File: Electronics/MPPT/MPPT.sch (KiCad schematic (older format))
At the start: 94 parts, among them J1 Solar Array, J2 Battery, J3 Car Power, J4 CAN_In, J5 CAN_Out, Q1 200N25N, Q2 200N25N, SW1 RESET, SW2 CAN Address, U1 PDS1-S12-S9-M, U2 Nucleo_L432KC, U3 UCC37321, U4 INA213, U5 ADM3055E, U6 INA213, U7 CDSOT23-T24CAN

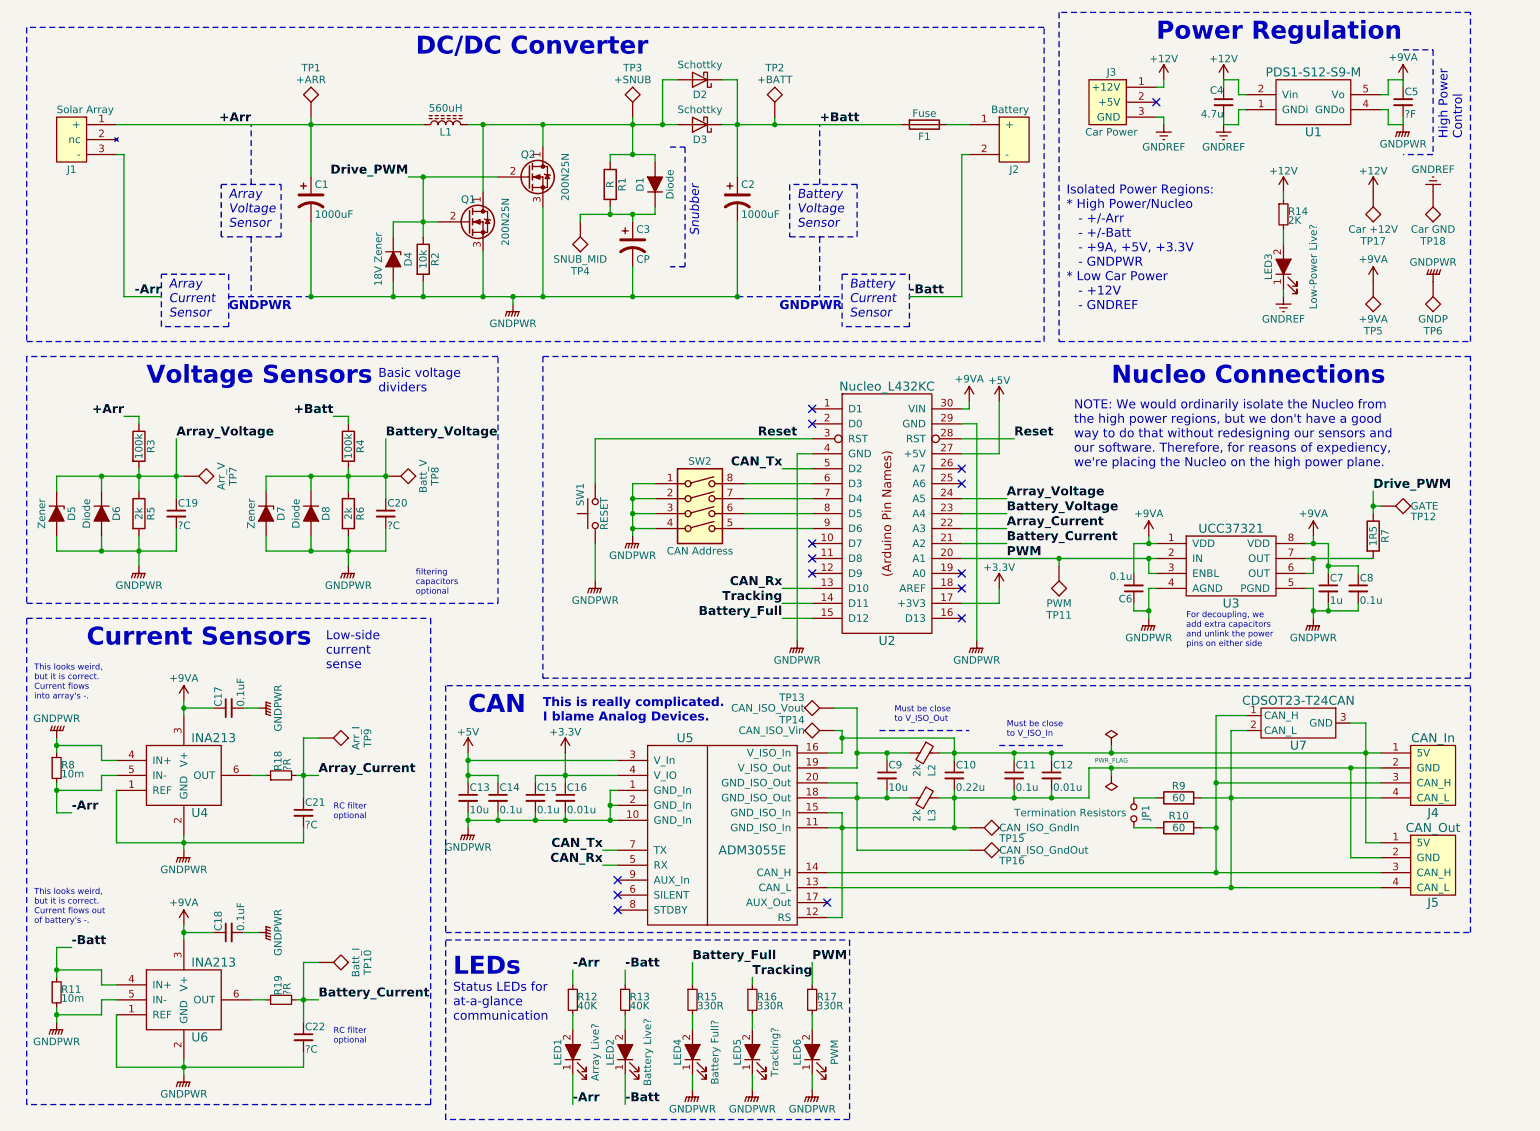
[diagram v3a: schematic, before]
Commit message: MPPT: Replaced power regulator with a 3W-output isolator.
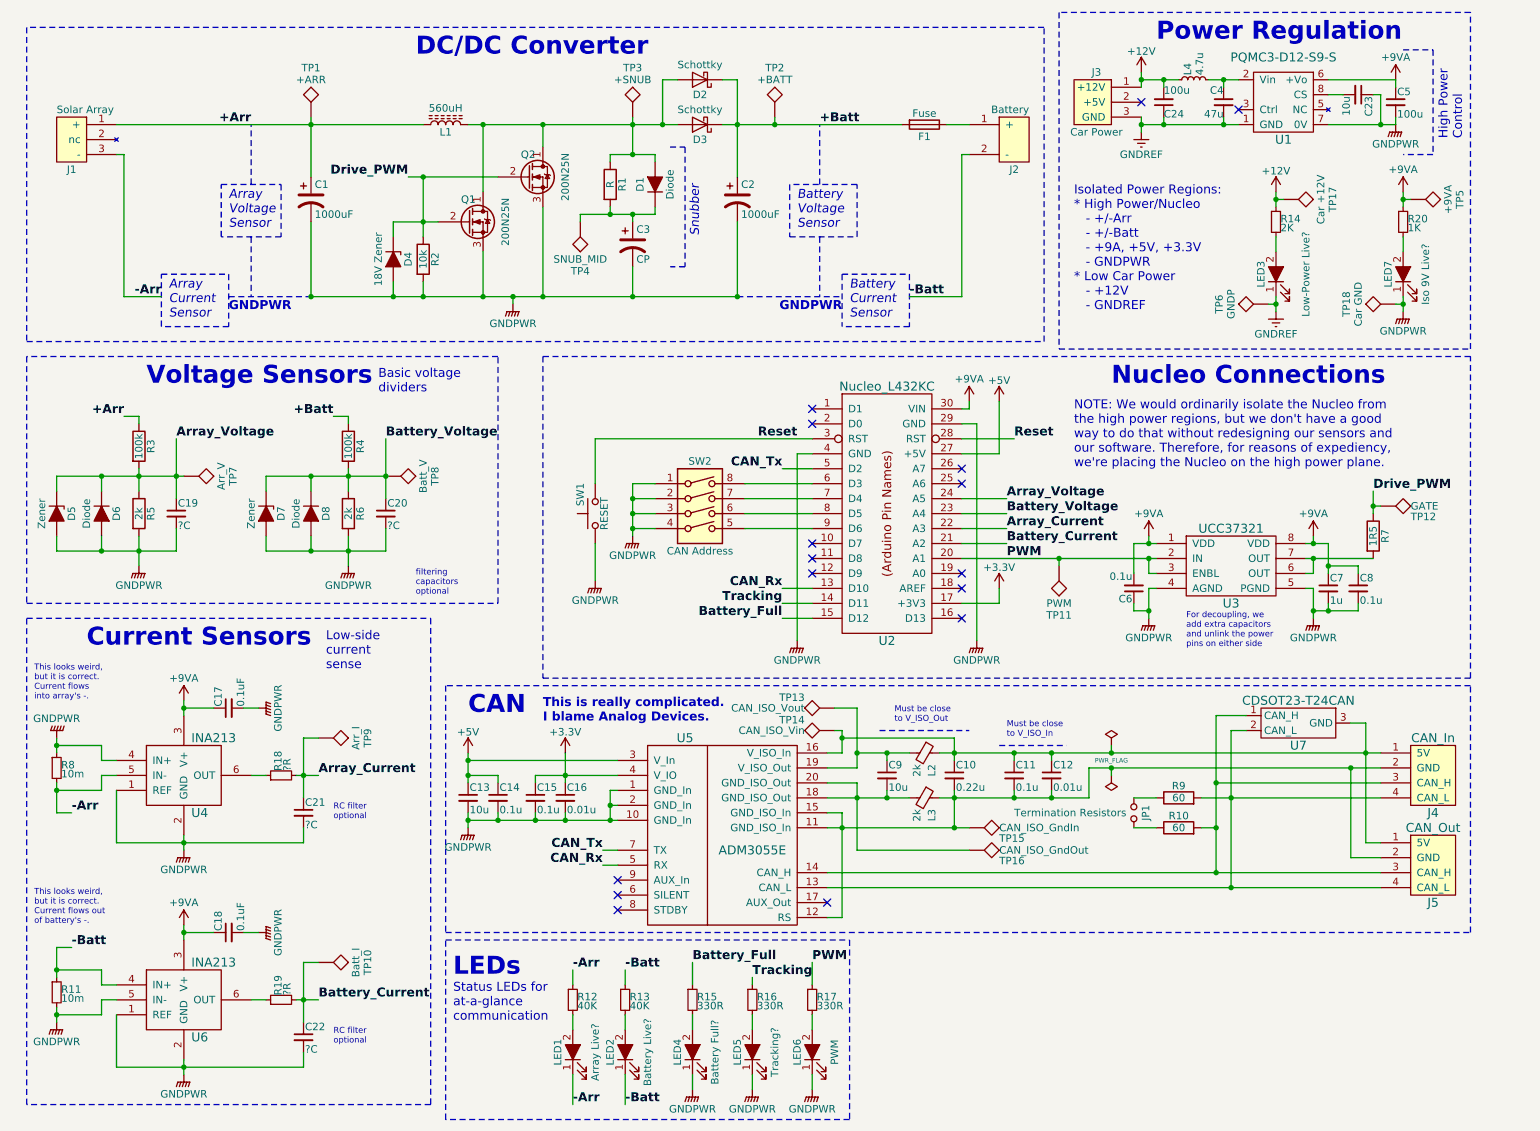
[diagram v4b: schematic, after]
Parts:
- removed U1: PDS1-S12-S9-M, UTSVT_ICs:PDS1-M, symbol PDS1-S12-S9-M
- added C23: 10u, Capacitors_SMD:C_0805_HandSoldering, symbol C_Small
- added C24: 100u, Capacitors_SMD:C_0805_HandSoldering, symbol C_Small
- added L4: 4.7u, Inductors_SMD:L_0805_HandSoldering, symbol L_Small
- added LED7: Iso 9V Live?, LEDs:LED_0805_HandSoldering, symbol LED_ALT
- added R20: 1K, Resistors_SMD:R_0805_HandSoldering, symbol R_Small
- added U1: PQMC3-D12-S9-S, UTSVT_ICs:CUI_PQMC3-S, symbol PQMC3-Dx-Sx-S
- C4: value 4.7u -> 47u
- C5: value ?F -> 100u
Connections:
- net +12V: now also C24.2, L4.1; no longer C4.1
- net +9VA: now also R20.1, U1.6 (+Vo)
- net GNDPWR: now also TP18.1, C23.1, LED7.1 (K), U1.7 (0V); no longer TP6.1
- net GNDREF: now also TP6.1, C24.1, U1.1 (GND); no longer TP18.1
- new net: C4.1, L4.2, U1.2 (Vin)
- new net: C23.2, U1.8 (CS)
- new net: LED7.2 (A), R20.2
- no-connect marks 15 -> 16
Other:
- moved on the sheet: C5, J3, LED3, R14, TP17, TP18, TP5, TP6

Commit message: MPPT: Clean up and rearrange schematic
* Compacted and cleaned up the CAN and Power Regulation blocks.
* Spread blocks out a little more
* Swapped locations of CAN and Nucleo Connections blocks to allow more space for the LEDs block to expand.
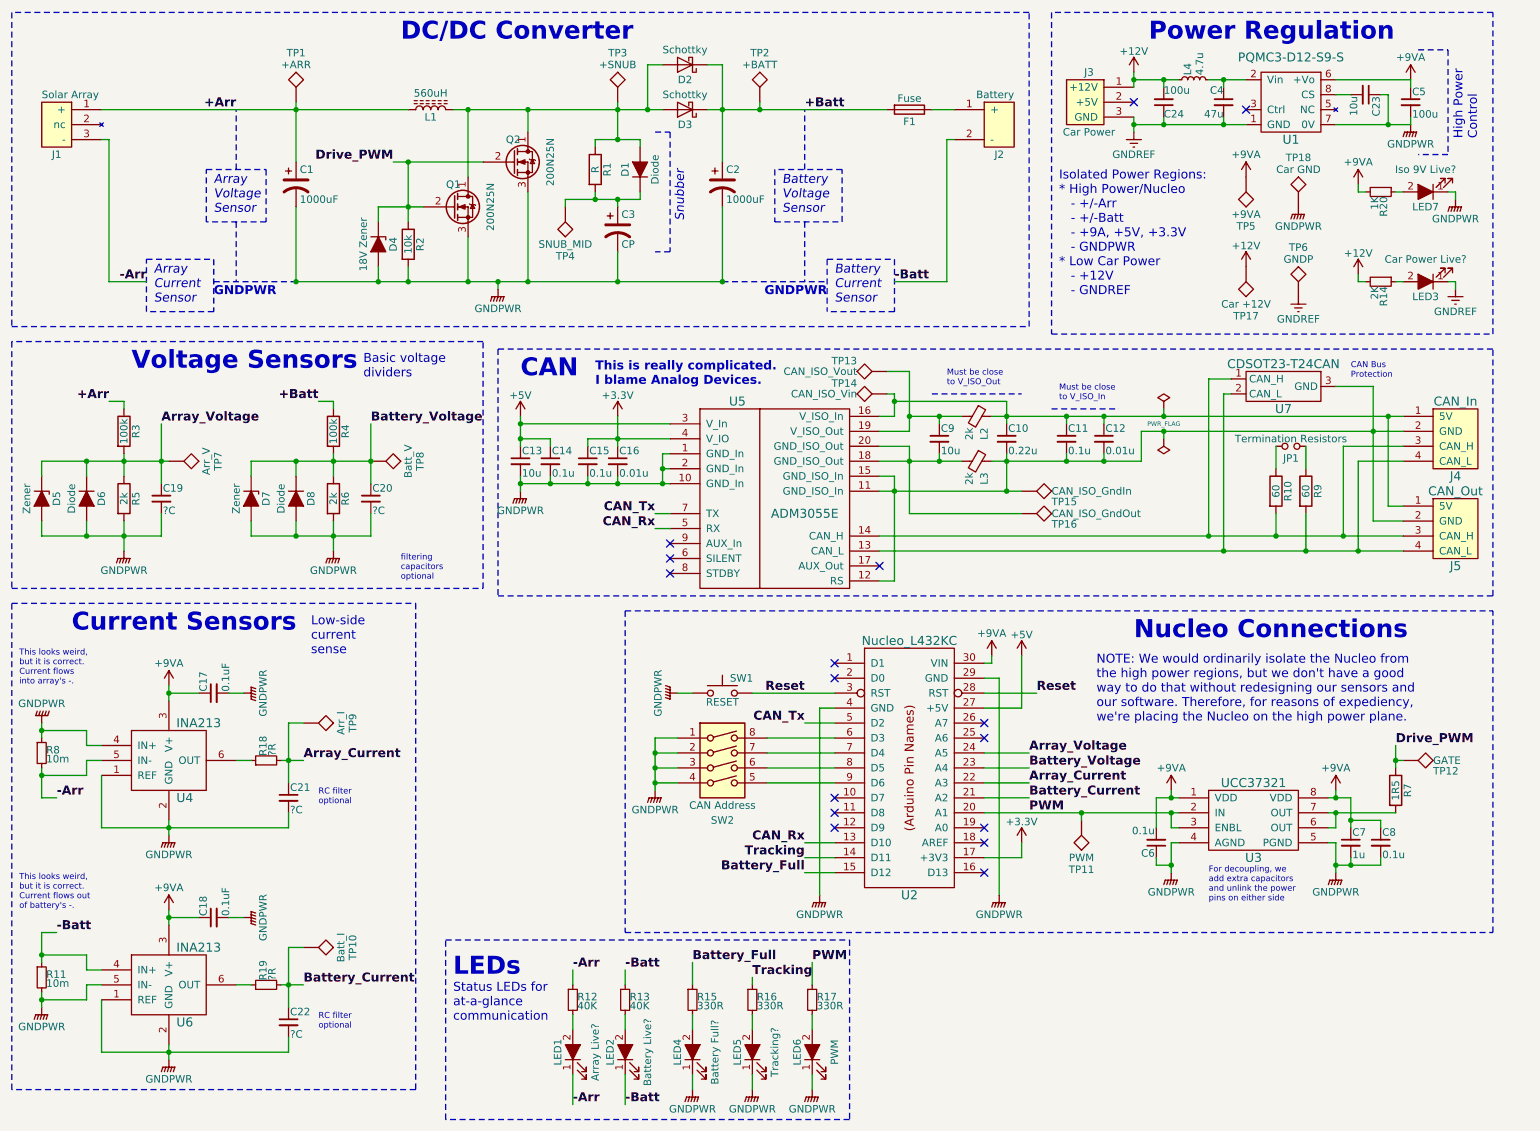
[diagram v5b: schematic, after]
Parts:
- LED3: value Low-Power Live? -> Car Power Live?
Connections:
- net +12V: now also R14.2; no longer R14.1
- net +9VA: now also R20.2; no longer R20.1
- net at C10.1, C11.1, C12.1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: no longer U7.3 (GND)
- net at C10.2, C11.2, C12.2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: now also U7.3 (GND)
- net at LED3.2 (A): now also R14.1; no longer R14.2
- net at LED7.2 (A): now also R20.1; no longer R20.2
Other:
- note added: "CAN Bus\nProtection"
- moved on the sheet: C1, C10, C11, C12, C13, C14, C15, C16, C17, C18, C19, C2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

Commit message: MPPT: Add CAN_Tx/Rx LEDs and TPs; move power LEDs to LEDs block
Also nudged some blocks and circuitry around.
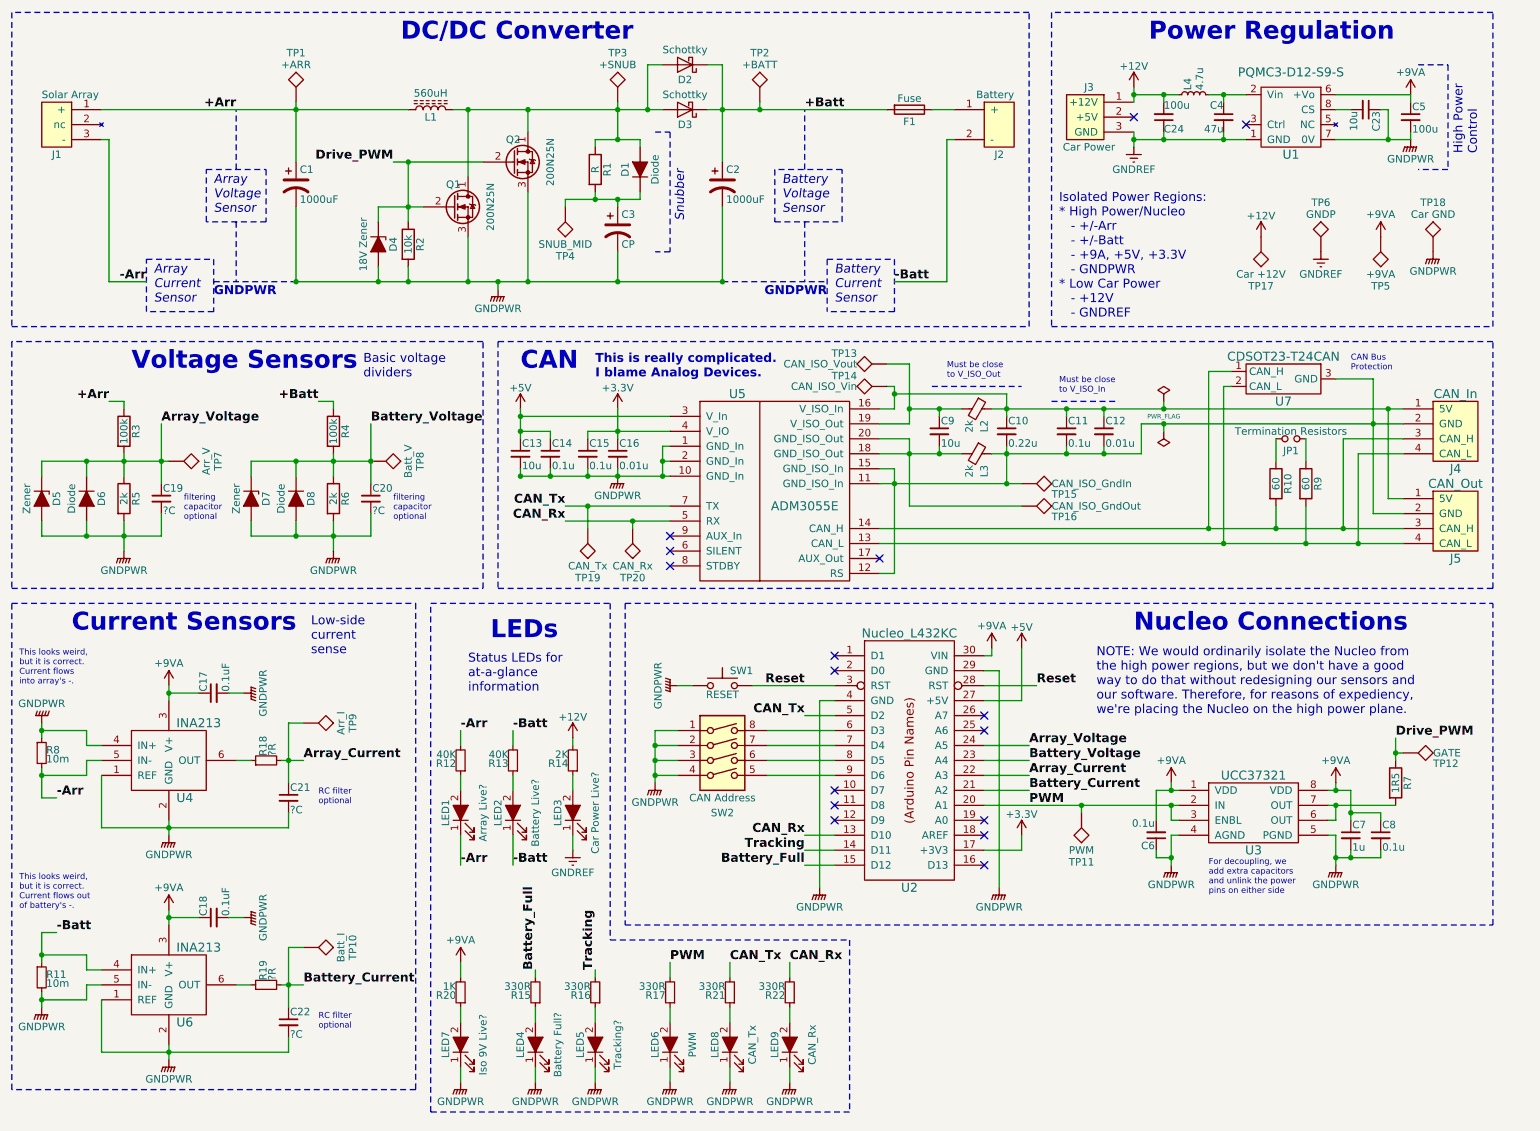
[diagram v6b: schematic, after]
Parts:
- added LED8: CAN_Tx, LEDs:LED_0805_HandSoldering, symbol LED_ALT
- added LED9: CAN_Rx, LEDs:LED_0805_HandSoldering, symbol LED_ALT
- added R21, R22: 330R, Resistors_SMD:R_0805_HandSoldering, symbol R_Small
- added TP19: CAN_Tx, Measurement_Points:Test_Point_Keystone_5005-5009_Compact, symbol TEST
- added TP20: CAN_Rx, Measurement_Points:Test_Point_Keystone_5005-5009_Compact, symbol TEST
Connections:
- net -Arr: now also R12.2; no longer R12.1
- net -Batt: now also R13.2; no longer R13.1
- net Battery_Full: now also R15.2; no longer R15.1
- net CAN_Rx: now also R22.2, TP20.1
- net CAN_Tx: now also R21.2, TP19.1
- net GNDPWR: now also LED8.1 (K), LED9.1 (K)
- net PWM: now also R17.2; no longer R17.1
- net Tracking: now also R16.2; no longer R16.1
- net at LED4.2 (A): now also R15.1; no longer R15.2
- net at LED5.2 (A): now also R16.1; no longer R16.2
- net at LED1.2 (A): now also R12.1; no longer R12.2
- net at LED2.2 (A): now also R13.1; no longer R13.2
- net at LED6.2 (A): now also R17.1; no longer R17.2
- new net: LED8.2 (A), R21.1
- new net: LED9.2 (A), R22.1
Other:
- note added: "Status LEDs for\nat-a-glance\ninformation"
- note added: "filtering\ncapacitor\noptional"
- note removed: "Status LEDs for\nat-a-glance\ncommunication"
- note removed: "\nfiltering\ncapacitors\noptional"
- moved on the sheet: C10, C11, C12, C13, C14, C15, C16, C23, C24, C4, C5, C6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
